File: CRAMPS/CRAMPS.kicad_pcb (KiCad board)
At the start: 2 copper layers, 99.1 x 99.1 mm, 192 parts, among them M101 PCB_GREEN_RMC, M102 LOGO_OSHW, P101 SOCKET_6_LONG, P102 HEADER_2, P103 HEADER_2, P201 PT_2,5-2-5,0-H, P202 KK-2.54-4W, P203 KK-2.54-4W, P204 KK-2.54-4W, P205 KK-2.54-4W, P206 KK-2.54-4W, P207 KK-2.54-4W, P208 POLOLU_SOCKET, P209 POLOLU_SOCKET, P210 POLOLU_SOCKET, P211 POLOLU_SOCKET, P301 HEADER_2, P302 KK-2.54-2W, P303 HEADER_4X2, P304 HEADER_3X2, P305 HEADER_6, P401 PT_2,5-2-5,0-H, P402 PT_2,5-2-5,0-H, P403 PT_2,5-2-5,0-H, P404 PT_1,5-3-3,5-H, P405 PT_1,5-2-3,5-H, P406 PT_1,5-2-3,5-H, P407 KK-2.54-2W, P408 PT_1,5-2-3,5-H, P409 KK-2.54-2W, P501 HEADER_6, P502 HEADER_6X2, P503 HEADER_4X2, P504 HEADER_4X2, P8 BB_EXP_CONN, P9 BB_EXP_CONN, Q101 2N7002K, Q301 2N7002K, Q302 2N7002K, Q303 2N7002K, Q304 2N7002K, Q305 2N7002K, Q401 IRLB8743PBF, Q402 IRLB8743PBF, Q403 IRLB8743PBF, Q404 DMN2075U, Q405 IRLB8743PBF, Q406 DMN2075U, SW101 SW_PUSH, SW102 SW_PUSH, U201 Pololu, U202 Pololu, U203 Pololu, U204 Pololu, U205 Pololu, U206 Pololu, U301 24C256, U302 74ACT244, U501 74CBTD3861

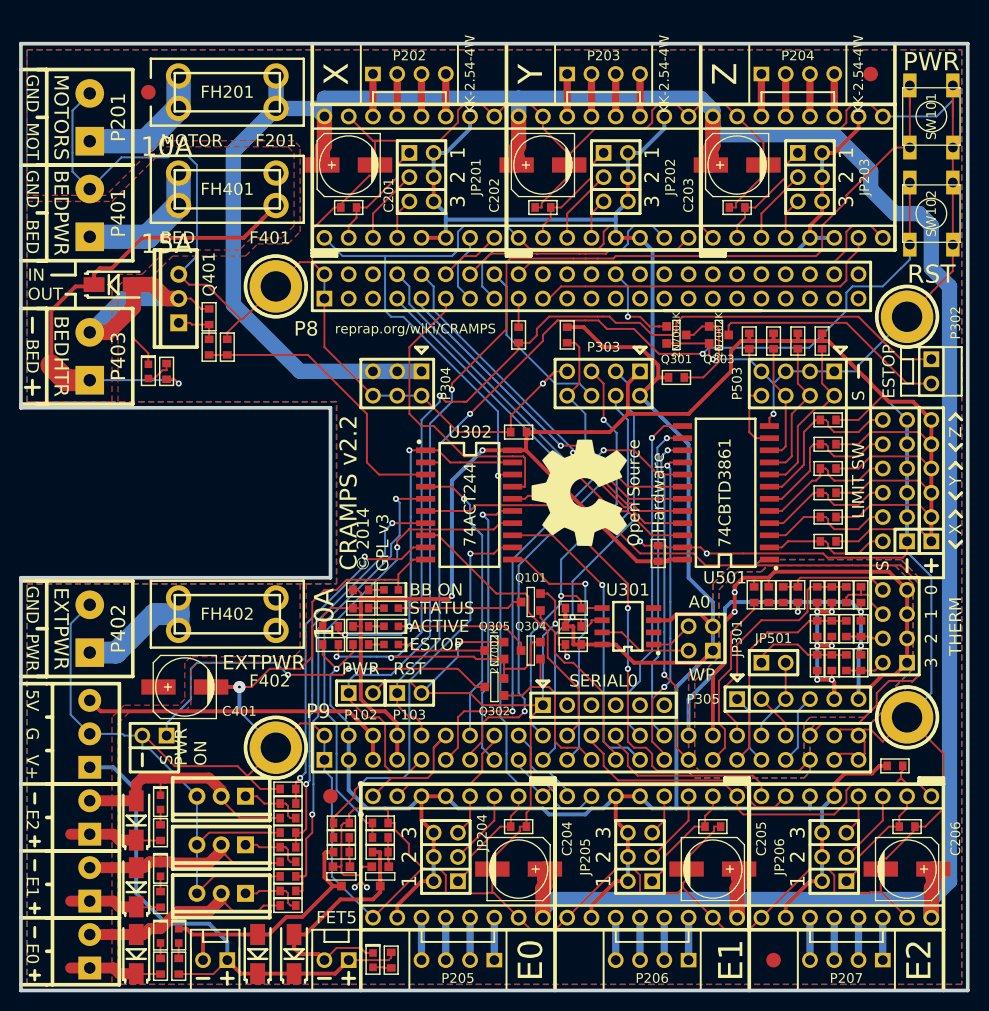
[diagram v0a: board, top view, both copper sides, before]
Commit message: updated the PCB with new netlist
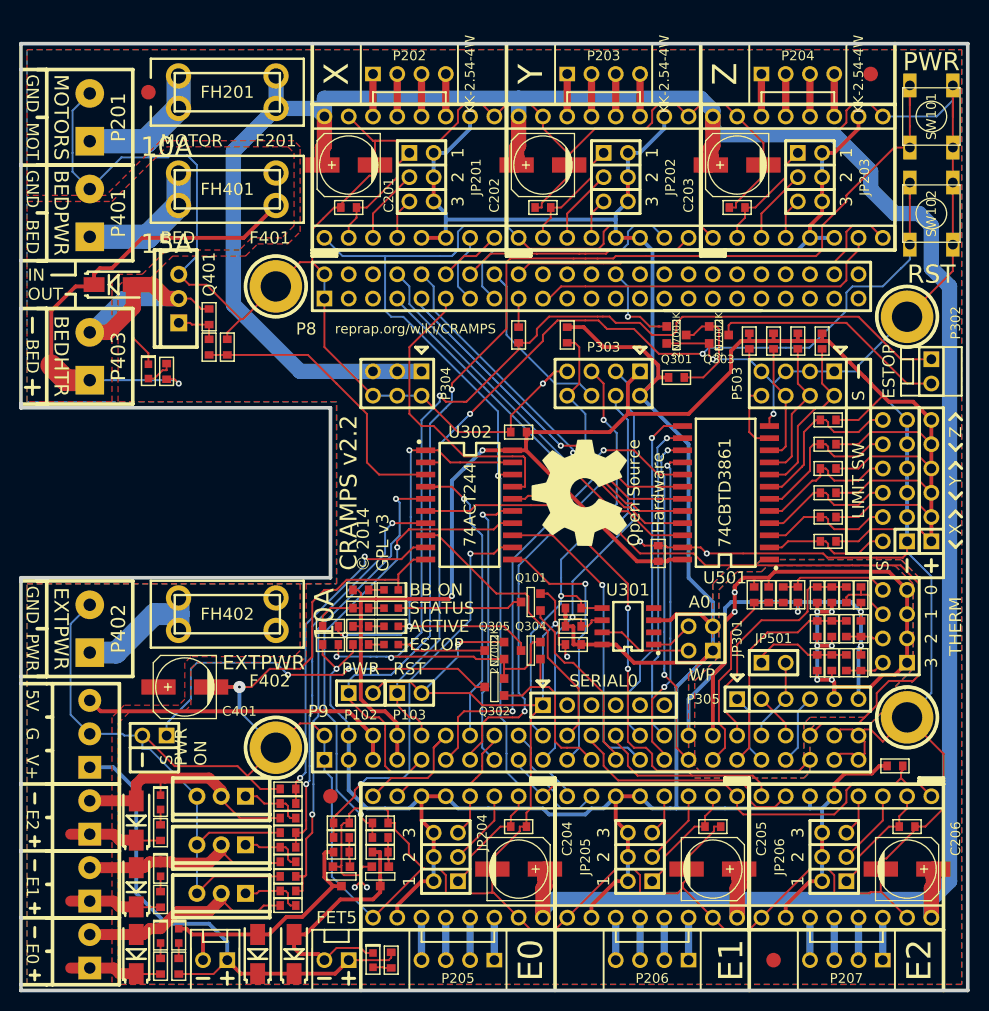
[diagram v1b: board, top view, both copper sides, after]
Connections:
- P101 pad 2: (no net) -> Net-(P101-Pad2)
- P101 pad 3: (no net) -> Net-(P101-Pad3)
- P101 pad 4: (no net) -> Net-(P101-Pad4)
- P101 pad 5: (no net) -> Net-(P101-Pad5)
- P101 pad 6: (no net) -> Net-(P101-Pad6)
- P8 pad 20: (no net) -> Net-(P8-Pad20)
- P8 pad 21: (no net) -> Net-(P8-Pad21)
- P8 pad 22: (no net) -> Net-(P8-Pad22)
- P8 pad 23: (no net) -> Net-(P8-Pad23)
- P8 pad 24: (no net) -> Net-(P8-Pad24)
- P8 pad 25: (no net) -> Net-(P8-Pad25)
- P8 pad 27: (no net) -> Net-(P8-Pad27)
- P8 pad 28: (no net) -> Net-(P8-Pad28)
- P8 pad 29: (no net) -> Net-(P8-Pad29)
- P8 pad 3: (no net) -> Net-(P8-Pad3)
- P8 pad 30: (no net) -> Net-(P8-Pad30)
- P8 pad 31: (no net) -> Net-(P8-Pad31)
- P8 pad 32: (no net) -> Net-(P8-Pad32)
- P8 pad 33: (no net) -> Net-(P8-Pad33)
- P8 pad 34: (no net) -> Net-(P8-Pad34)
- P8 pad 35: (no net) -> Net-(P8-Pad35)
- P8 pad 36: (no net) -> Net-(P8-Pad36)
- P8 pad 37: (no net) -> Net-(P8-Pad37)
- P8 pad 38: (no net) -> Net-(P8-Pad38)
- P8 pad 39: (no net) -> Net-(P8-Pad39)
- P8 pad 4: (no net) -> Net-(P8-Pad4)
- P8 pad 40: (no net) -> Net-(P8-Pad40)
- P8 pad 41: (no net) -> Net-(P8-Pad41)
- P8 pad 42: (no net) -> Net-(P8-Pad42)
- P8 pad 43: (no net) -> Net-(P8-Pad43)
- P8 pad 44: (no net) -> Net-(P8-Pad44)
- P8 pad 45: (no net) -> Net-(P8-Pad45)
- P8 pad 46: (no net) -> Net-(P8-Pad46)
- P8 pad 5: (no net) -> Net-(P8-Pad5)
- P8 pad 6: (no net) -> Net-(P8-Pad6)
- U301 pad 2: (no net) -> Net-(U301-Pad2)
